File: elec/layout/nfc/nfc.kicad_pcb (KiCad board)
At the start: 2 copper layers, 27 parts, among them U1 _NXP_Semicon_PN5321A3HN_C106_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

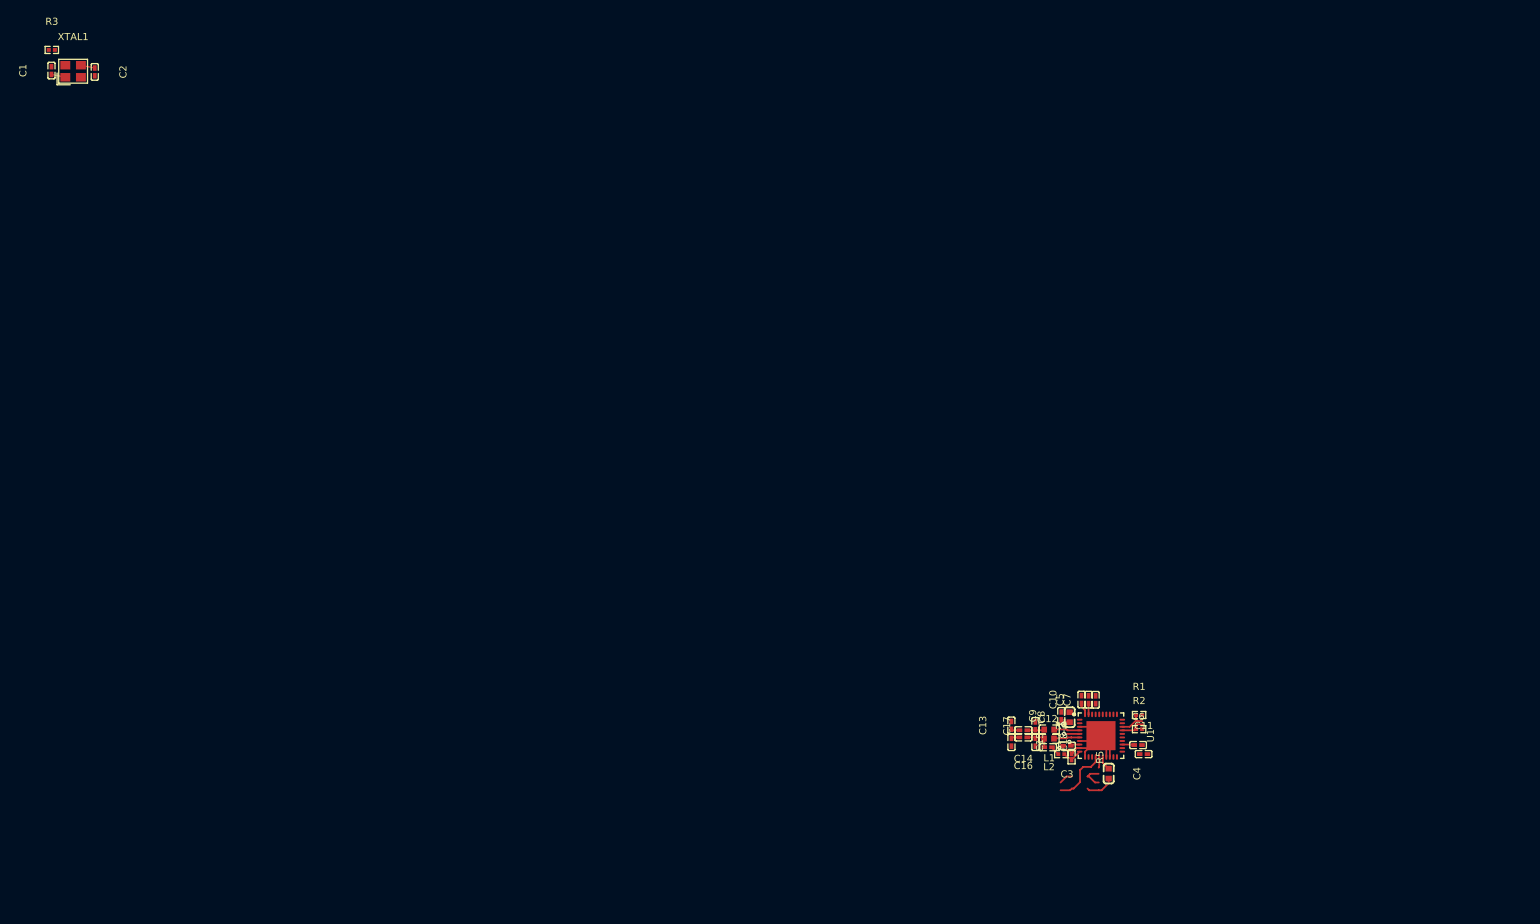
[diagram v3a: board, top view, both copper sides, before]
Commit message: import antenna and button footprints
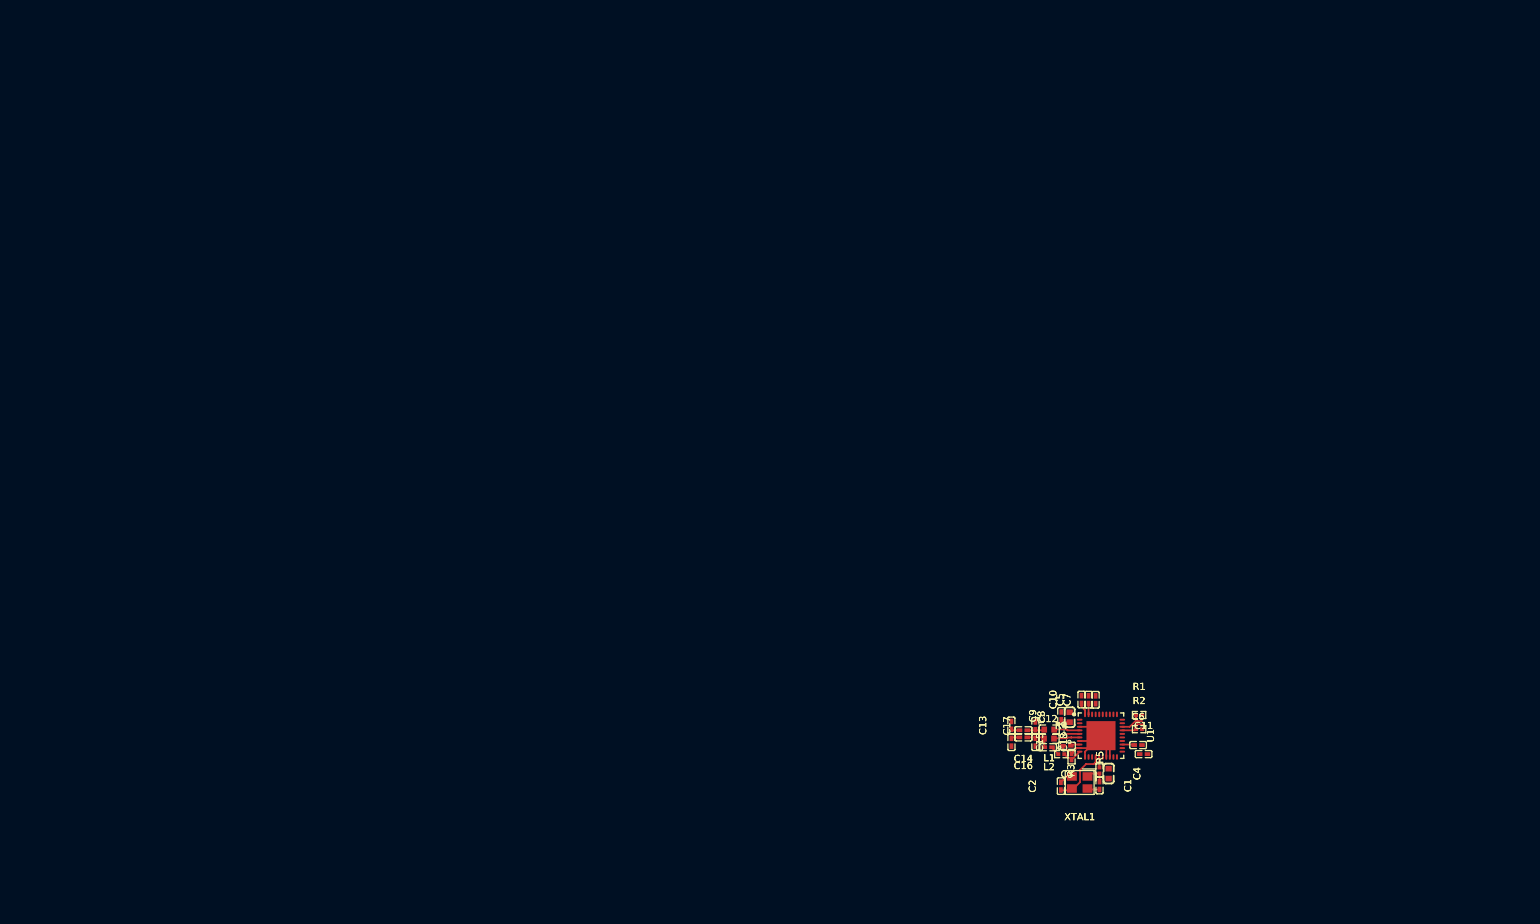
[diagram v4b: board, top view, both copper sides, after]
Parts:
- moved R3 179.1 mm to (144.6, 98.5), turned to 90 degrees
- moved C1 178.7 mm to (144.6, 100.6), turned to -90 degrees
- moved XTAL1 173.6 mm to (141.8, 100.2), turned to 180 degrees
- moved C2 169.3 mm to (139.2, 100.7), turned to 90 degrees
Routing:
- net net-2: track 2.75 -> 29.9 mm, vias 0 -> 1
- net net-1: track 31.9 -> 12.3 mm, vias 1 -> 3
- net net-5: track 14.3 -> 1.49 mm, vias 3 -> 0
- net net-8: track 4.67 -> 1.57 mm
- net net-7: track 1.20 -> 3.96 mm
- net oscillator-net: track 5.66 -> 3.22 mm
- net net-9: track 1.55 -> 3.91 mm
- net net-3: track 10.3 -> 8.31 mm
- net net-11: track 3.66 -> 2.75 mm
- net net-4: track 3.96 -> 4.67 mm

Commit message: builds working
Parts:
- C1, C16, C2: value (none) -> 20pF ±5% 50V C0G
- C10, C12, C3, C5, C6, C7, C9: value (none) -> 100nF ±10% 16V X7R
- C15: value (none) -> 100pF ±5% 50V C0G
- C18: value (none) -> 220pF ±10% 50V X7R
- C8: value (none) -> 10µF ±10% 10V X5R
- L2: value (none) -> 560nH ±5% 450mA 480mΩ
- R1: value 10Ω ±1% 62.5mW -> 5.1kΩ ±1% 62.5mW
- R2, R3, R5: value (none) -> 5.1kΩ ±1% 62.5mW
- moved R3 179.1 mm to (-3.00, -3.00), turned to 0 degrees
- moved C1 178.7 mm to (-3.05, -0.10), turned to 90 degrees
- moved XTAL1 173.6 mm to (0.00, 0.00), turned to 0 degrees
- moved C2 169.3 mm to (3.05, 0.10), turned to 270 degrees
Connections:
- net rstout_n renamed signal
- C1 pad 2: net-2 -> net-1
- C10 pad 1: net-1 -> net-6
- C10 pad 2: net-2 -> net-1
- C11 pad 1: net-2 -> net-1
- C12 pad 2: net-8 -> net-3
- C13 pad 1: net-6 -> net
- C13 pad 2: net-2 -> net-1
- C14 pad 2: net-6 -> net
- C15 pad 2: net-2 -> net-1
- C17 pad 2: net-2 -> net-1
- C18 pad 2: net-2 -> net-1
- C2 pad 1: net-3 -> net-9
- C2 pad 2: net-2 -> net-1
- C3 pad 1: net-1 -> net-6
- C3 pad 2: net-2 -> net-1
- C4 pad 1: net-1 -> net-6
- C4 pad 2: net-2 -> net-1
- C5 pad 1: net-1 -> net-6
- C5 pad 2: net-2 -> net-1
- C6 pad 1: net-1 -> net-6
- C6 pad 2: net-2 -> net-1
- C7 pad 1: net -> net-5
- C8 pad 1: net-1 -> net-6
- C8 pad 2: net-2 -> net-1
- C9 pad 1: net-1 -> net-6
- C9 pad 2: net-2 -> net-1
- L1 pad 2: net-7 -> net-2
- L2 pad 2: net-9 -> net-8
- R1 pad 1: net-4 -> net-10
- R2 pad 1: net-10 -> net-7
- R3 pad 2: net-5 -> net-11
- R4 pad 1: net-8 -> net-3
- R4 pad 2: net-11 -> net-4
- R5 pad 1: net-2 -> net-1
- R5 pad 2: net-11 -> net-4
- U1 pad 1: net-2 -> net-1
- U1 pad 10: net-11 -> net-4
- U1 pad 11: net-2 -> net-1
- U1 pad 14: net-3 -> net-9
- U1 pad 15: net-5 -> net-11
- U1 pad 16: net-1 -> net-6
- U1 pad 17: net-2 -> net-1
- U1 pad 18: net-2 -> net-1
- U1 pad 23: net-1 -> net-6
- U1 pad 27: net-10 -> net-7
- U1 pad 28: net-4 -> net-10
- U1 pad 3: net-2 -> net-1
- U1 pad 37: net -> net-5
- U1 pad 39: net-1 -> net-6
- U1 pad 4: net-7 -> net-2
- U1 pad 40: net-1 -> net-6
- U1 pad 41: net-2 -> net-1
- U1 pad 5: net-1 -> net-6
- U1 pad 6: net-9 -> net-8
- U1 pad 7: net-2 -> net-1
- U1 pad 8: net-1 -> net-6
- U1 pad 9: net-2 -> net-1
- XTAL1 pad 2: net-2 -> net-1
- XTAL1 pad 3: net-3 -> net-9
- XTAL1 pad 4: net-2 -> net-1
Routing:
- net oscillator-net: track 3.22 -> 5.21 mm
- net net-9: track 3.91 -> 5.90 mm

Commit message: Build full
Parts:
- C1, C2: value 20pF ±5% 50V C0G -> 100nF ±10% 50V X7R; footprint lcsc:C0402 -> lcsc:C0603
- C10, C11, C3, C5, C6, C7, C9: value 100nF ±10% 16V X7R -> 100nF ±10% 50V X7R; footprint lcsc:C0402 -> lcsc:C0603
- C4, C8: value 10µF ±10% 10V X5R -> 100nF ±10% 50V X7R
- L1, L2: value 560nH ±5% 450mA 480mΩ -> 560nH ±5% infHz 450mA 480mΩ
- R1, R2, R3, R5: value 5.1kΩ ±1% 62.5mW -> 1kΩ ±1% 100mW; footprint lcsc:R0402 -> lcsc:R0603
- moved C1 0.15 mm to (-3.05, -0.25)
- moved C2 0.15 mm to (3.05, 0.25)
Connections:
- net power_vmid-lv renamed lv
- C10 pad 1: net-6 -> net
- C12 pad 2: net-3 -> net-13
- C13 pad 1: net -> net-11
- C14 pad 2: net -> net-11
- C15 pad 1: net-12 -> net-6
- C16 pad 2: net-12 -> net-6
- C2 pad 1: net-9 -> net-5
- C3 pad 1: net-6 -> net
- C4 pad 1: net-6 -> net
- C5 pad 1: net-6 -> net
- C6 pad 1: net-6 -> net
- C7 pad 1: net-5 -> net-2
- C7 pad 2: power_svdd-lv -> net-1
- C8 pad 1: net-6 -> net
- C9 pad 1: net-6 -> net
- L1 pad 2: net-2 -> net-10
- L2 pad 2: net-8 -> net-9
- R1 pad 1: net-10 -> net-7
- R1 pad 2: hv -> net-12
- R2 pad 1: net-7 -> net-8
- R2 pad 2: hv -> net-12
- R3 pad 2: net-11 -> net-4
- R4 pad 1: net-3 -> net-13
- R4 pad 2: net-4 -> net-3
- R5 pad 2: net-4 -> net-3
- U1 pad 10: net-4 -> net-3
- U1 pad 14: net-9 -> net-5
- U1 pad 15: net-11 -> net-4
- U1 pad 16: net-6 -> net
- U1 pad 20: nfc_ic-net -> nfc_ic.footprint.pins[12].net-net
- U1 pad 21: nfc_ic-net -> nfc_ic.footprint.pins[13].net-net
- U1 pad 22: nfc_ic-net -> nfc_ic.footprint.pins[14].net-net
- U1 pad 23: net-6 -> net
- U1 pad 25: p70_irq -> signal
- U1 pad 26: signal -> signal-1
- U1 pad 27: net-7 -> net-8
- U1 pad 28: net-10 -> net-7
- U1 pad 37: net-5 -> net-2
- U1 pad 39: net-6 -> net
- U1 pad 4: net-2 -> net-10
- U1 pad 40: net-6 -> net
- U1 pad 5: net-6 -> net
- U1 pad 6: net-8 -> net-9
- U1 pad 8: net-6 -> net
- XTAL1 pad 3: net-9 -> net-5
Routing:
- net net-5: track 1.49 -> 3.48 mm
- net net-9: track 5.90 -> 3.91 mm

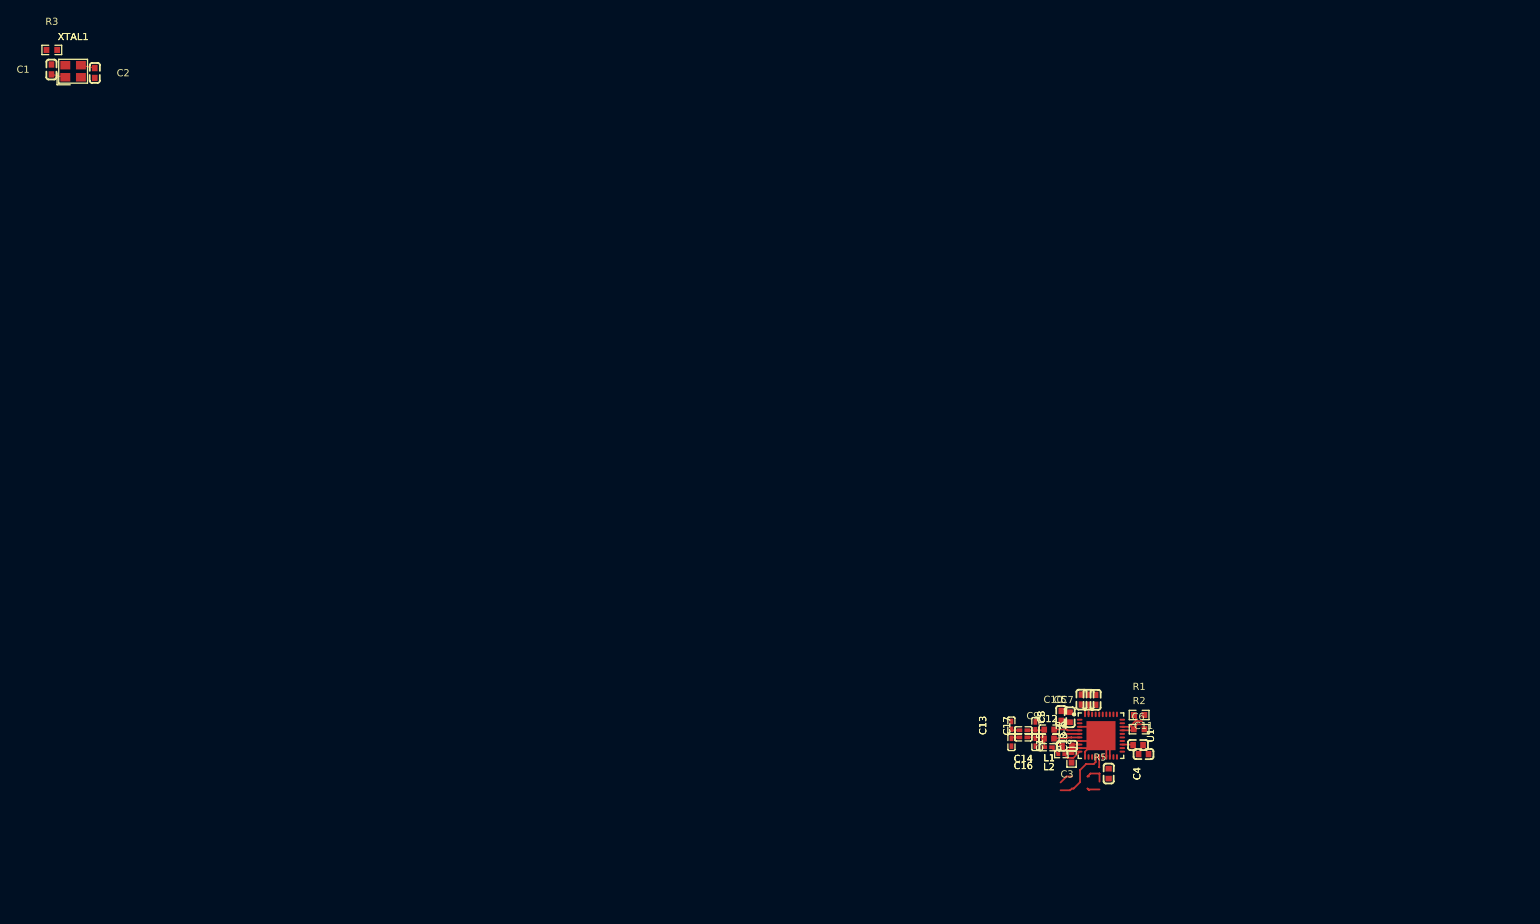
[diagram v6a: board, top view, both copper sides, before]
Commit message: Don't update PCB files
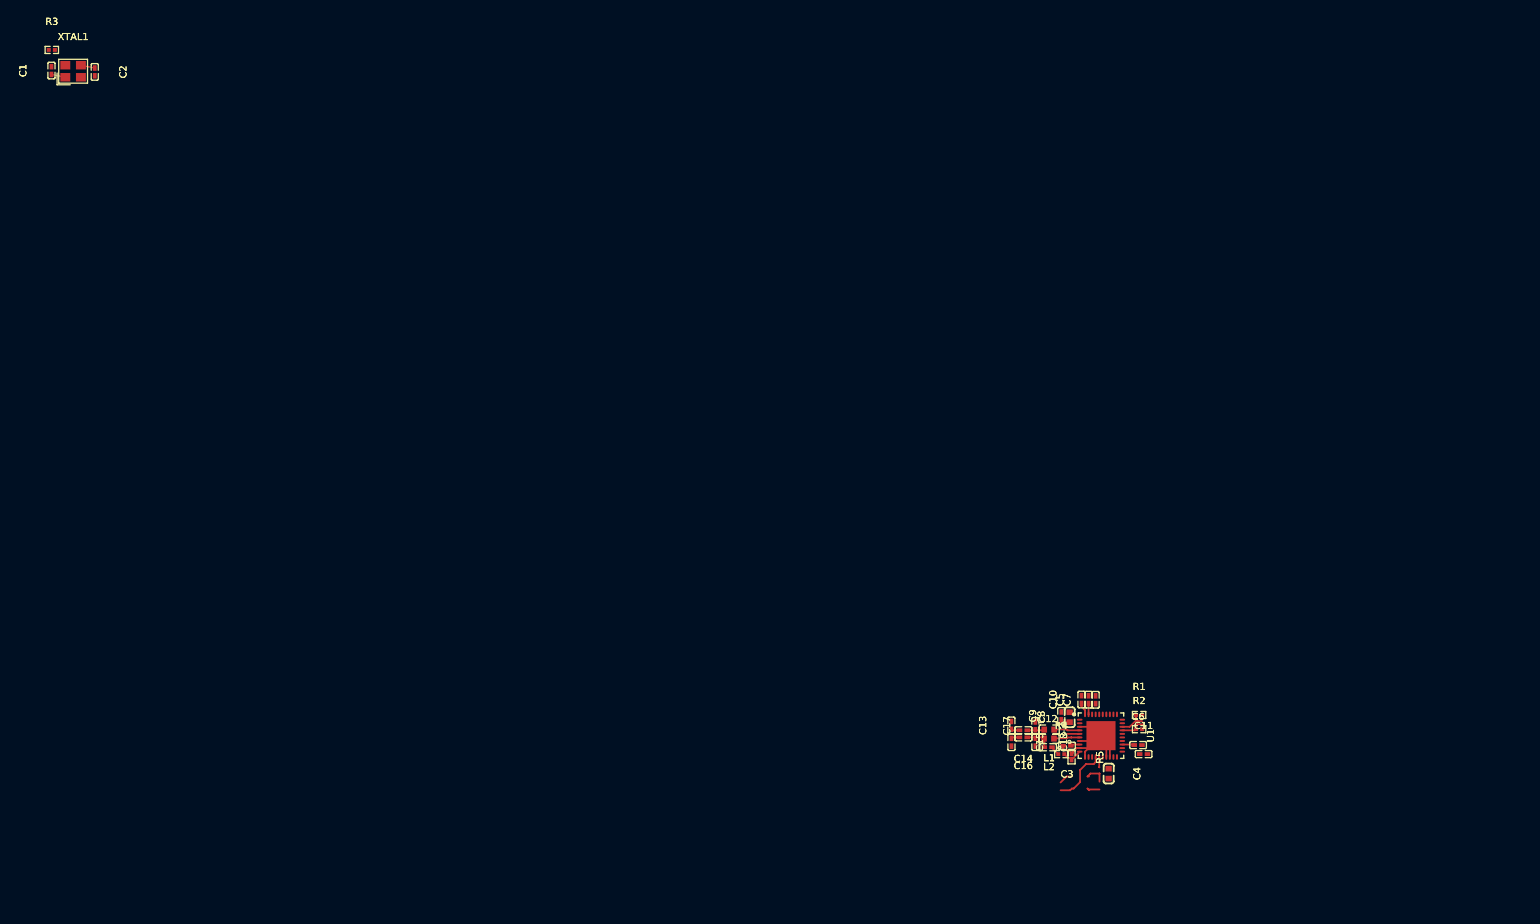
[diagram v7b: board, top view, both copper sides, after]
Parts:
- C1, C2: value 100nF ±10% 50V X7R -> 20pF ±5% 50V C0G; footprint lcsc:C0603 -> lcsc:C0402
- C10, C11, C3, C5, C6, C7, C9: value 100nF ±10% 50V X7R -> 100nF ±10% 16V X7R; footprint lcsc:C0603 -> lcsc:C0402
- C4, C8: value 100nF ±10% 50V X7R -> 10µF ±10% 10V X5R
- L1, L2: value 560nH ±5% infHz 450mA 480mΩ -> 560nH ±5% 450mA 480mΩ
- R1, R2, R3, R5: value 1kΩ ±1% 100mW -> 5.1kΩ ±1% 62.5mW; footprint lcsc:R0603 -> lcsc:R0402
- moved C1 0.15 mm to (-3.05, -0.10)
- moved C2 0.15 mm to (3.05, 0.10)
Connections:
- net lv renamed power_vmid-lv
- C10 pad 1: net -> net-6
- C12 pad 2: net-13 -> net-3
- C13 pad 1: net-11 -> net
- C14 pad 2: net-11 -> net
- C15 pad 1: net-6 -> net-12
- C16 pad 2: net-6 -> net-12
- C2 pad 1: net-5 -> net-9
- C3 pad 1: net -> net-6
- C4 pad 1: net -> net-6
- C5 pad 1: net -> net-6
- C6 pad 1: net -> net-6
- C7 pad 1: net-2 -> net-5
- C7 pad 2: net-1 -> power_svdd-lv
- C8 pad 1: net -> net-6
- C9 pad 1: net -> net-6
- L1 pad 2: net-10 -> net-2
- L2 pad 2: net-9 -> net-8
- R1 pad 1: net-7 -> net-10
- R1 pad 2: net-12 -> hv
- R2 pad 1: net-8 -> net-7
- R2 pad 2: net-12 -> hv
- R3 pad 2: net-4 -> net-11
- R4 pad 1: net-13 -> net-3
- R4 pad 2: net-3 -> net-4
- R5 pad 2: net-3 -> net-4
- U1 pad 10: net-3 -> net-4
- U1 pad 14: net-5 -> net-9
- U1 pad 15: net-4 -> net-11
- U1 pad 16: net -> net-6
- U1 pad 20: nfc_ic.footprint.pins[12].net-net -> nfc_ic-net
- U1 pad 21: nfc_ic.footprint.pins[13].net-net -> nfc_ic-net
- U1 pad 22: nfc_ic.footprint.pins[14].net-net -> nfc_ic-net
- U1 pad 23: net -> net-6
- U1 pad 25: signal -> p70_irq
- U1 pad 26: signal-1 -> signal
- U1 pad 27: net-8 -> net-7
- U1 pad 28: net-7 -> net-10
- U1 pad 37: net-2 -> net-5
- U1 pad 39: net -> net-6
- U1 pad 4: net-10 -> net-2
- U1 pad 40: net -> net-6
- U1 pad 5: net -> net-6
- U1 pad 6: net-9 -> net-8
- U1 pad 8: net -> net-6
- XTAL1 pad 3: net-5 -> net-9
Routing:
- net net-5: track 3.48 -> 1.49 mm
- net net-9: track 3.91 -> 5.90 mm

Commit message: Update PCB version to kicad9; Disable non-existing builds
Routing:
- net net-2: track 29.9 -> 8.00 mm, vias 1 -> 0
- net net-1: track 12.3 -> 25.8 mm, vias 3 -> 1
- net net-6: track 1.20 -> 12.3 mm, vias 0 -> 3
- net net-3: track 8.31 -> 1.57 mm
- net net-9: track 5.90 -> 10.3 mm
- net net-8: track 1.57 -> 3.91 mm
- net net-4: track 4.67 -> 2.75 mm
- net net-5: track 1.49 -> 0.00 mm
- net net-11: track 2.75 -> 1.49 mm
- net net: track 0.00 -> 1.20 mm
- net net-10: track 3.66 -> 4.67 mm
